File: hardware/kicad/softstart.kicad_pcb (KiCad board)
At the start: 4 copper layers, 160 x 100 mm, 101 parts, among them J1 AC_IN, J2 AC_OUT, J3 SWD, Q1 IRFB4110, Q2 IRFB4110, Q3 AO3400, Q4 AO3400, U1 STM32G031F6P6, U2 H11AA1, U3 AMS1117-3.3, U4 INA180A1

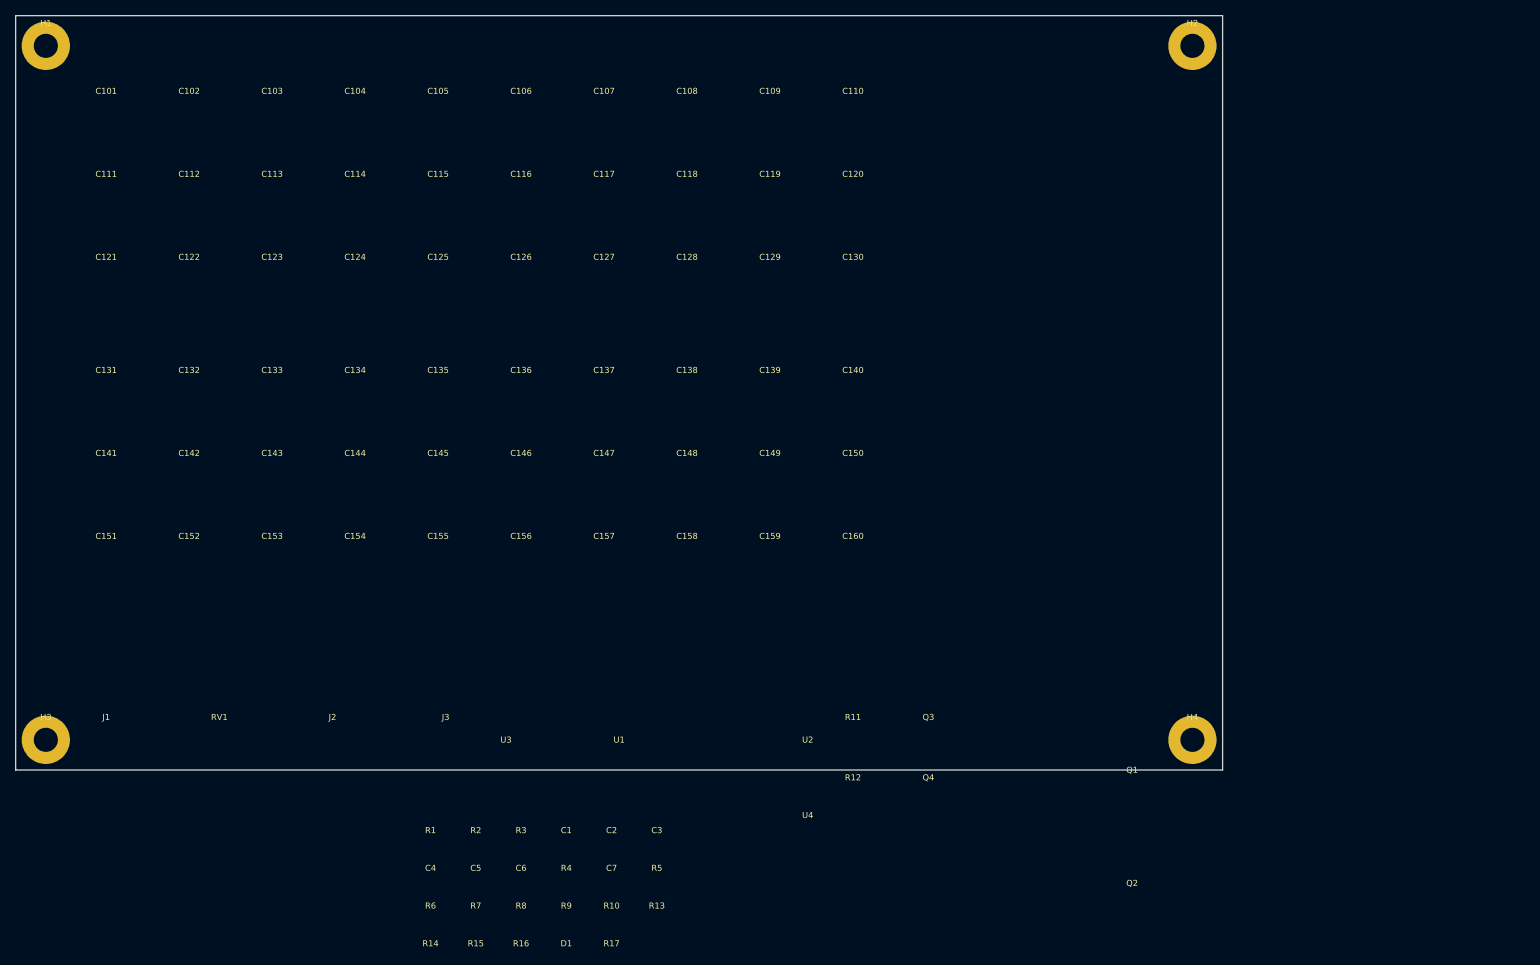
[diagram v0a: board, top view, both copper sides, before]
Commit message: Fix ERC violations in schematic generator
Reduce ERC errors from 271 to 6 (5 intentional design choices):
- Fix bridge rectifier pin references (use pin numbers not names)
- Fix T-junction wiring by breaking vertical buses into segments
- Add no-connect flags for unused MCU pins (PC15, PB9/PC14)
- Wire gate driver IN- pins to GND and connect OUTL parallel to OUTH
- Fix 4-terminal Kelvin shunt resistor wiring
- Add PWR_FLAG on GND rail for proper power annotation
- Move bypass cap GND bus left to avoid crossing MCU signal wires

Remaining errors are intentional: L7812→LDO cascade, gate driver
parallel outputs (OUTH/OUTL).

Co-Authored-By: Claude Opus 4.5 <noreply@anthropic.com>
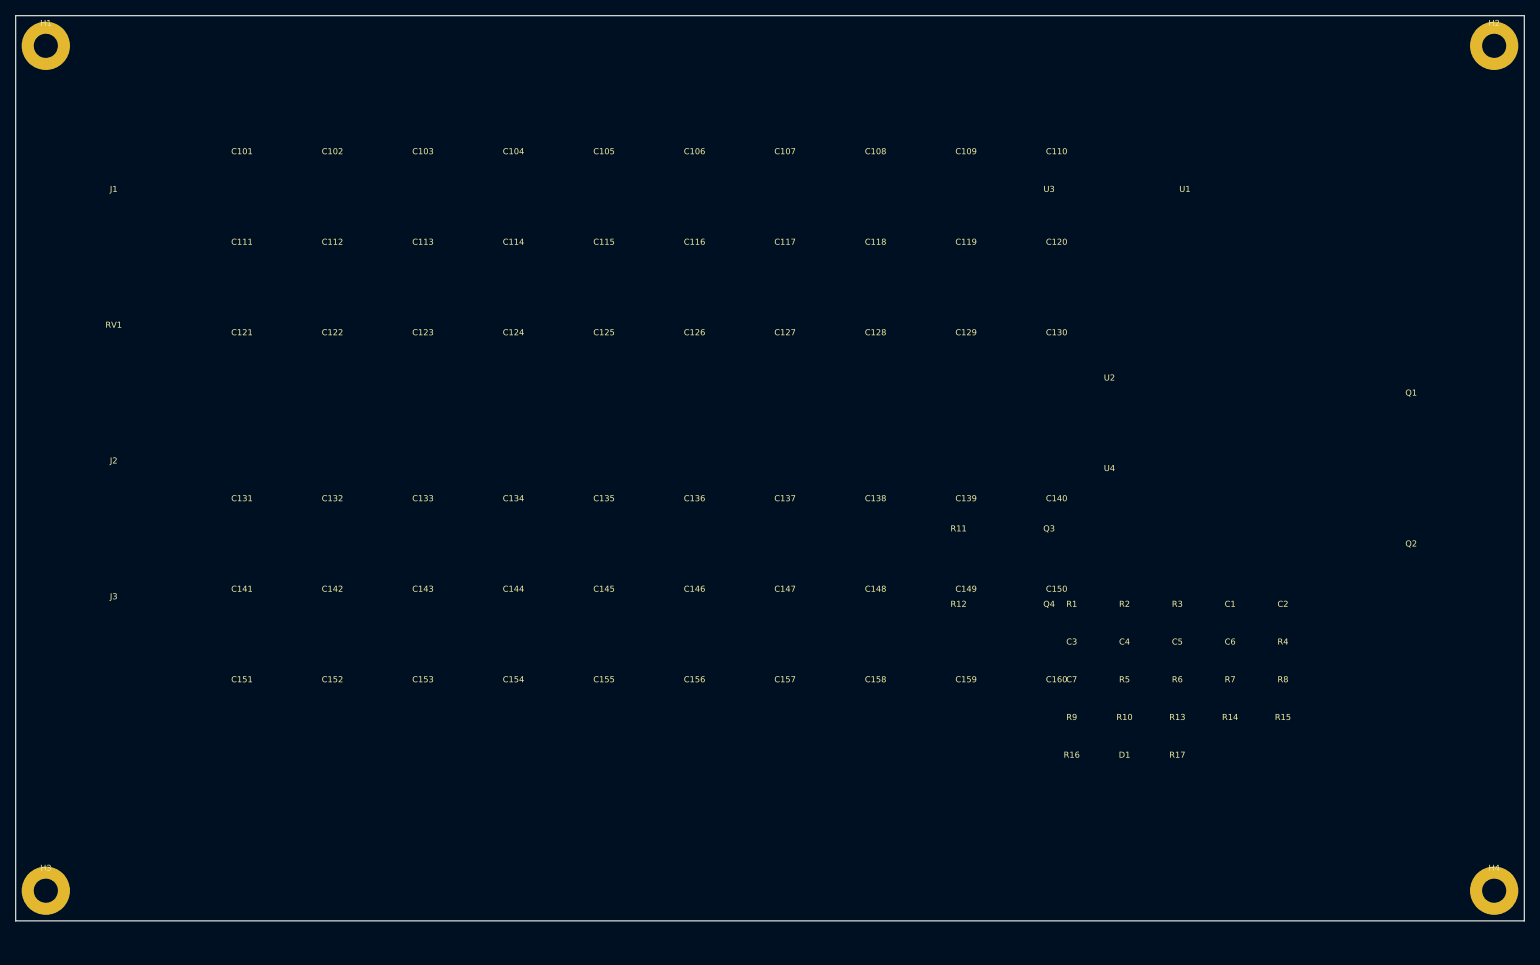
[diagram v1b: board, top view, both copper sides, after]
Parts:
- moved R15 111.1 mm to (168.0, 95.0)
- moved R14 110.2 mm to (161.0, 95.0)
- moved R8 105.4 mm to (168.0, 90.0)
- moved U1 104.7 mm to (155.0, 25.0)
- moved R7 104.4 mm to (161.0, 90.0)
- moved R6 103.4 mm to (154.0, 90.0)
- moved U3 102.5 mm to (137.0, 25.0)
- moved R4 99.6 mm to (168.0, 85.0)
- moved C6 98.7 mm to (161.0, 85.0)
- moved C5 97.7 mm to (154.0, 85.0)
- moved C4 96.8 mm to (147.0, 85.0)
- moved C2 93.9 mm to (168.0, 80.0)
- moved C1 93.0 mm to (161.0, 80.0)
- moved R3 92.0 mm to (154.0, 80.0)
- moved R2 91.1 mm to (147.0, 80.0)
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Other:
- board size 160 x 100 mm -> 200 x 120 mm
- copper layers 4 -> 2
